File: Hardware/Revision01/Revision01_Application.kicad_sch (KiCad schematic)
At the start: 74 parts, among them J21 StrainConn, J22 StrainConn, J23 StrainConn, J24 StrainConn, J25 StrainConn, J26 StrainConn, J27 StrainConn, J28 StrainConn, J4 Conn_01x03, Q3 NMOS, Q4 PMOS, Q6 PMOS, U2 MRF89XAM9AT-I/RM, U4 ICM-45605

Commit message: random stuff added
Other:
- note added: "https://www.digikey.ca/en/products/detail/analog-devices-inc/ADA4254ARUZ-R7/11483491"
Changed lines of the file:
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@@
+		)
+	)
+	(text "https://www.digikey.ca/en/products/detail/analog-devices-inc/ADA4254ARUZ-R7/11483491\n"
+		(exclude_from_sim no)
+		(at 70.358 205.232 0)
+		(effects
+			(font
+				(size 1.4986 1.4986)
+			)
 		)
 	)

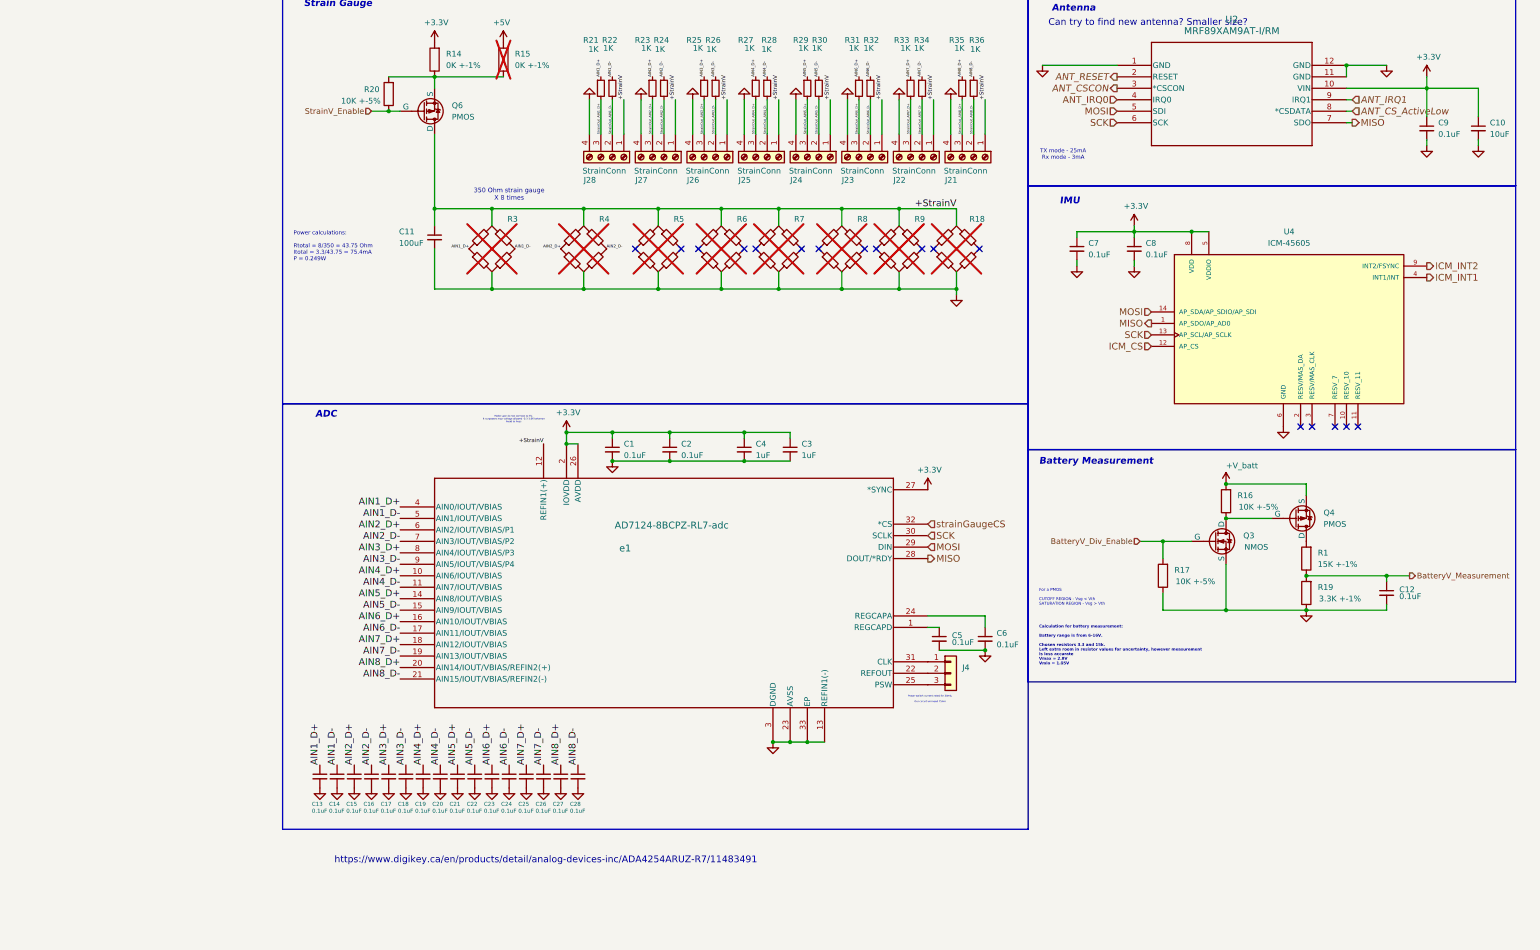
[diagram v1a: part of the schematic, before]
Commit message: some feedback implemented, MISO/MOSI SIWTCHED, GPIO_USB_5V FIXED, COMMENTS REGARDING ALTERNATIVE ADC's, and PCB CONNECTED TO EXTERNAL GND added
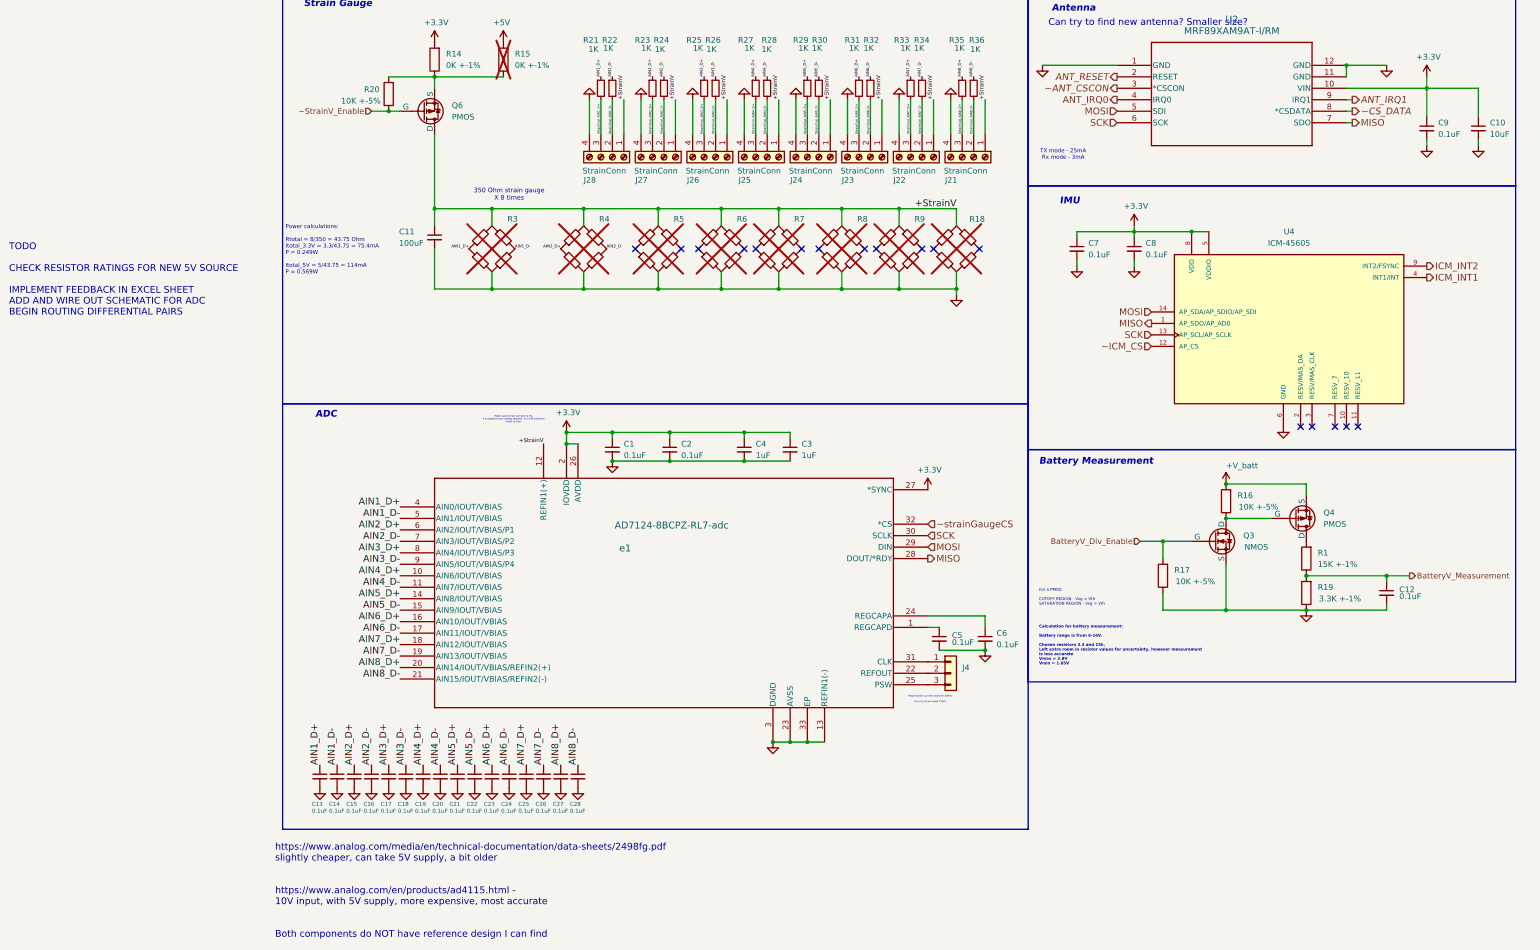
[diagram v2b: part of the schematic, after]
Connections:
- net ANT_CSCON renamed ~ANT_CSCON
- net ANT_CS_ActiveLow renamed ~CS_DATA
- net ICM_CS renamed ~ICM_CS
- net StrainV_Enable renamed ~StrainV_Enable
- net strainGaugeCS renamed ~strainGaugeCS
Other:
- note added: "Power calculations: Rtotal = 8/350 = 43.75 Ohm Itotal_3.3V = 3.3/43.75 = 75.4mA P = 0.249W Itotal_5V = 5/43.75 = 114mA P = 0.569W"
- note added: "TODO CHECK RESISTOR RATINGS FOR NEW 5V SOURCE IMPLEMENT FEEDBACK IN EXCEL SHEET ADD AND WIRE OUT SCHEMATIC FOR ADC BEGIN ROUTING DIFFERENTIAL PAIRS"
- note added: "https://www.analog.com/media/en/technical-documentation/data-sheets/2498fg.pdf slightly cheaper, can take 5V supply, a bit older https://www.analog.com/en/products/ad4115.html - 10V input, with 5V supply, more expensive, most accurate Both components do NOT have reference design I can find"
- note removed: "Power calculations: Rtotal = 8/350 = 43.75 Ohm Itotal = 3.3/43.75 = 75.4mA P = 0.249W"
- note removed: "https://www.digikey.ca/en/products/detail/analog-devices-inc/ADA4254ARUZ-R7/11483491"
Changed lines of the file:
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@@
+		)
+	)
+	(text "https://www.analog.com/media/en/technical-documentation/data-sheets/2498fg.pdf\nslightly cheaper, can take 5V supply, a bit older\n\n\nhttps://www.analog.com/en/products/ad4115.html - \n10V input, with 5V supply, more expensive, most accurate\n\n\nBoth components do NOT have reference design I can find\n"
+		(exclude_from_sim no)
+		(at 10.414 212.09 0)
+		(effects
+			(font
+				(size 1.4986 1.4986)
+			)
+			(justify left)
 		)
 	)
@@
 			(font
 				(size 1.016 1.016)
-			)
-		)
-	)
-	(text "https://www.digikey.ca/en/products/detail/analog-devices-inc/ADA4254ARUZ-R7/11483491\n"
-		(exclude_from_sim no)
-		(at 70.358 205.232 0)
-		(effects
-			(font
-				(size 1.4986 1.4986)
 			)
 		)
@@
 		)
 	)
-	(text "Power calculations:\n\nRtotal = 8/350 = 43.75 Ohm\nItotal = 3.3/43.75 = 75.4mA\nP = 0.249W"
+	(text "Power calculations:\n\nRtotal = 8/350 = 43.75 Ohm\nItotal_3.3V = 3.3/43.75 = 75.4mA\nP = 0.249W\n\nItotal_5V = 5/43.75 = 114mA\nP = 0.569W"
 		(exclude_from_sim no)
-		(at 14.478 69.342 0)
+		(at 12.7 70.104 0)
 		(effects
 			(font
@@
 				(size 1.4986 1.4986)
 			)
+		)
+	)
+	(text "TODO\n\nCHECK RESISTOR RATINGS FOR NEW 5V SOURCE\n\nIMPLEMENT FEEDBACK IN EXCEL SHEET\nADD AND WIRE OUT SCHEMATIC FOR ADC\nBEGIN ROUTING DIFFERENTIAL PAIRS"
+		(exclude_from_sim no)
+		(at -48.514 76.708 0)
+		(effects
+			(font
+				(size 1.4986 1.4986)
+			)
+			(justify left)
 		)
 	)
@@
 		)
 	)
-	(hierarchical_label "ANT_CS_ActiveLow"
-		(shape input)
+	(hierarchical_label "~CS_DATA"
+		(shape output)
 		(at 248.92 39.37 0)
 		(effects
@@
 	)
 	(hierarchical_label "ANT_IRQ1"
-		(shape input)
+		(shape output)
 		(at 248.92 36.83 0)
 		(effects
@@
 		)
 	)
-	(hierarchical_label "StrainV_Enable"
+	(hierarchical_label "~StrainV_Enable"
 		(shape input)
 		(at 31.75 39.37 180)
@@
 		)
 	)
-	(hierarchical_label "strainGaugeCS"
+	(hierarchical_label "~strainGaugeCS"
 		(shape input)
 		(at 154.94 130.81 0)
@@
 		)
 	)
-	(hierarchical_label "ICM_CS"
+	(hierarchical_label "~ICM_CS"
 		(shape input)
 		(at 204.47 91.44 180)
@@
 	)
 	(hierarchical_label "ANT_IRQ0"
-		(shape input)
+		(shape output)
 		(at 196.85 36.83 180)
 		(effects
@@
 		)
 	)
-	(hierarchical_label "ANT_CSCON"
+	(hierarchical_label "~ANT_CSCON"
 		(shape output)
 		(at 196.85 34.29 180)

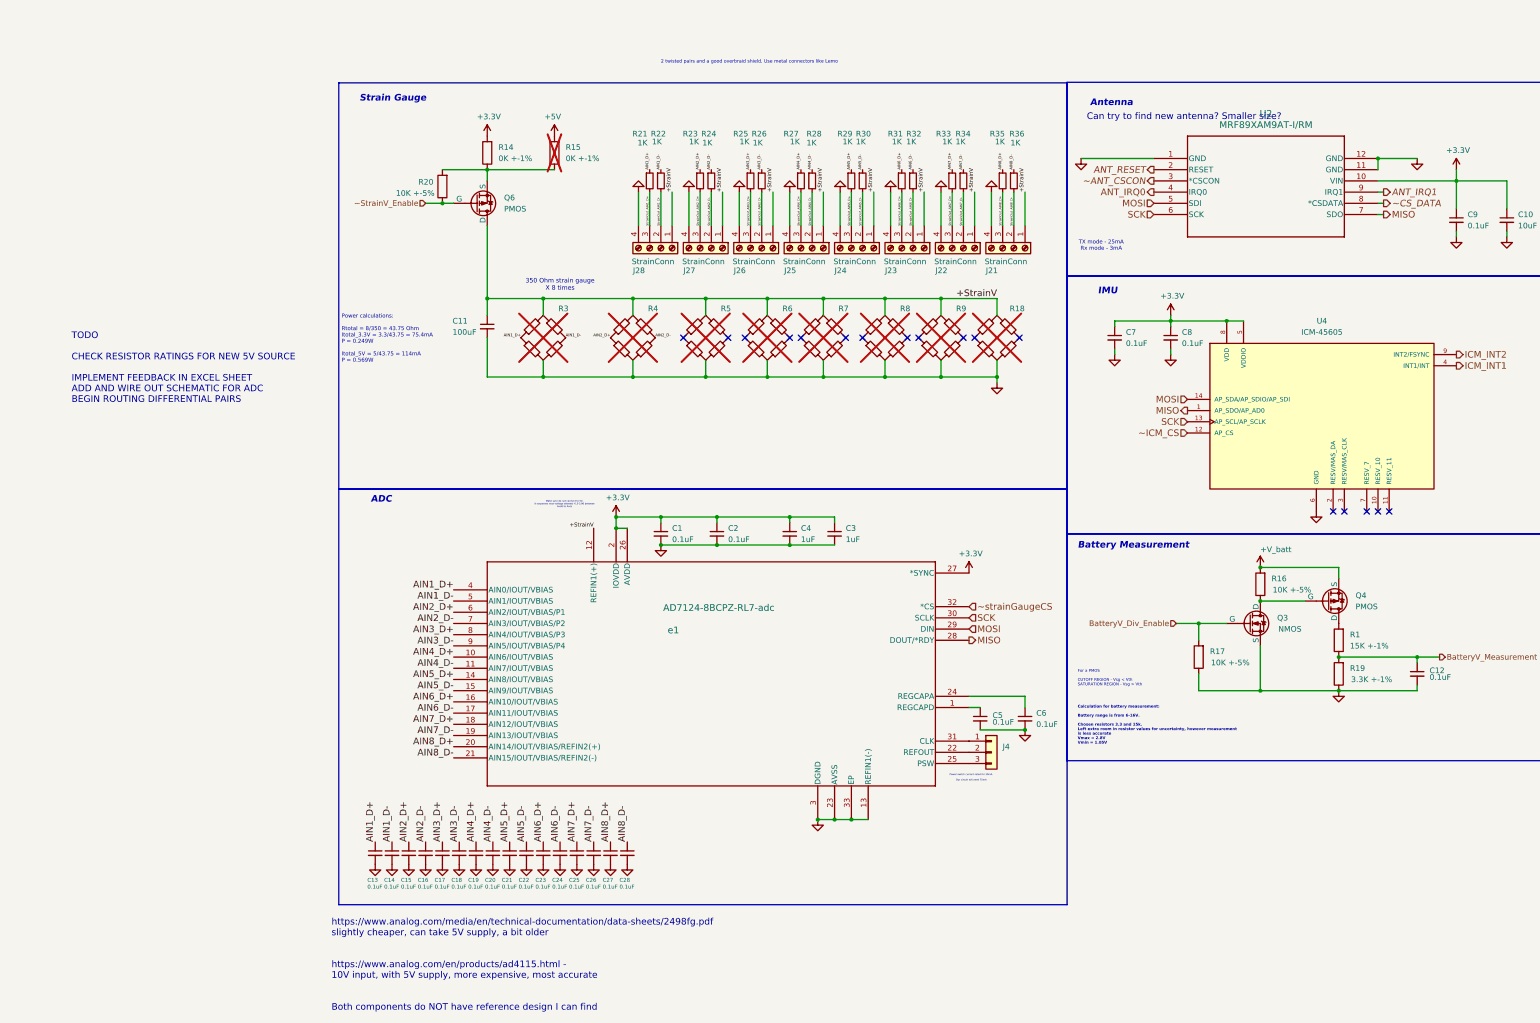
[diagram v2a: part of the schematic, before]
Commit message: Implemented new more reliable design utilizing instrumentation amplifiers
Changed RESISTORS for new Power requirements
Added prototype features of breathing cube to test out.
Removed MCU sheet, as moving pins around was getting too messy
Picked out Instrumentation OP-AMP, INA331 or INA2331
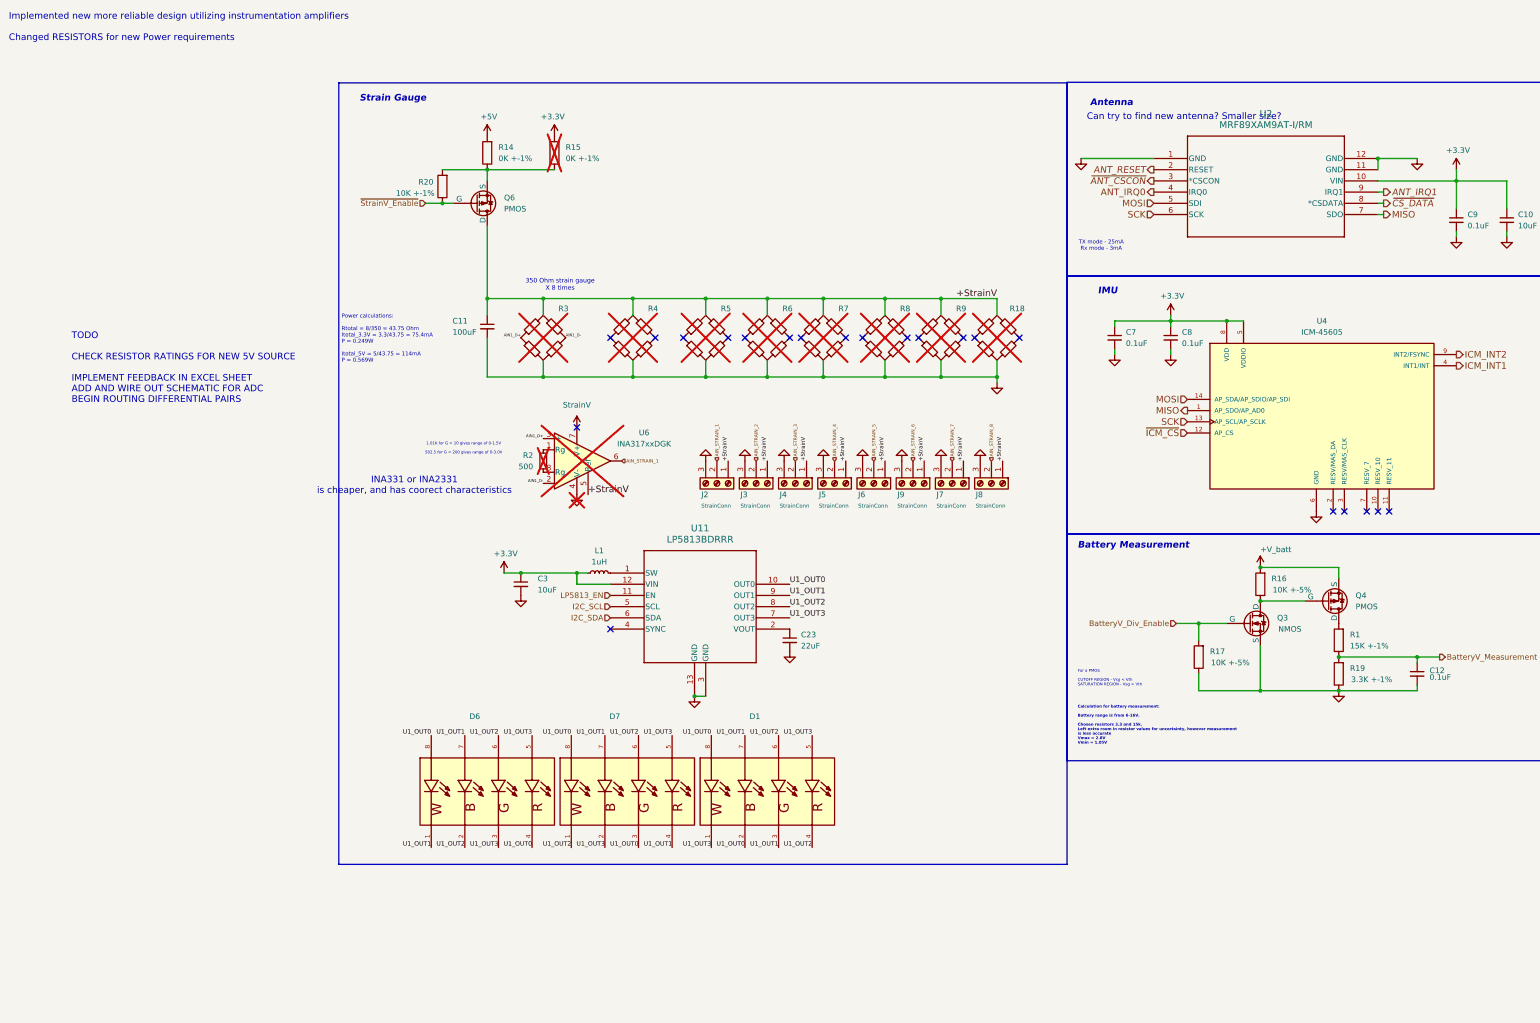
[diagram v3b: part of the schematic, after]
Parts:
- removed C1, C13, C14, C15, C16, C17, C18, C19, C2, C20, C21, C22, C24, C25, C26, C27, C28, C5, C6: 0.1uF, Capacitor_SMD:C_0402_1005Metric_Pad0.74x0.62mm_HandSolder, symbol Device:C_Small
- removed C4: 1uF, Capacitor_SMD:C_0805_2012Metric, symbol Device:C_Small
- removed J21, J22, J23, J24, J25, J26, J27, J28: StrainConn, 691137710004:691137710004, symbol Connector:Screw_Terminal_01x04
- removed J4: Conn_01x03, Connector_PinHeader_2.54mm:PinHeader_1x03_P2.54mm_Vertical, symbol Connector_Generic:Conn_01x03
- removed R21, R22, R23, R24, R25, R26, R27, R28, R29, R30, R31, R32, R33, R34, R35, R36: 1K, Resistor_SMD:R_0402_1005Metric_Pad0.72x0.64mm_HandSolder, symbol Device:R_Small
- removed e1: AD7124-8BCPZ-RL7-adc, AD7124-8BCPZ-RL7-adc:CP-32-12_ADI-L, symbol AD7124-8BCPZ-RL7-adc:AD7124-8BCPZ-RL7
- added D1, D6, D7: RGBW_LED, RGBW:SOL120P540X160-8N, symbol RGBW LED:OSFW4BS8C1A
- added J2, J3, J4, J5, J6, J7, J8, J9: StrainConn, 691137710003:691137710003, symbol Connector:Screw_Terminal_01x03
- added L1: 1uH, Inductor_SMD:L_0201_0603Metric_Pad0.64x0.40mm_HandSolder, symbol Device:L_Small
- added R2: 500, Resistor_SMD:R_0603_1608Metric_Pad0.98x0.95mm_HandSolder, symbol Device:R_Small
- added U11: LP5813BDRRR, Package_SON:WSON-12-1EP_3x3mm_P0.5mm_EP1.5x2.5mm, symbol LP5813BD:LP5813BDRRR
- added U6: INA317xxDGK, Package_SO:VSSOP-8_3x3mm_P0.65mm, symbol INA317:INA333xxDGK
- C23: value 0.1uF -> 22uF; footprint Capacitor_SMD:C_0402_1005Metric_Pad0.74x0.62mm_HandSolder -> Capacitor_SMD:C_0603_1608Metric_Pad1.08x0.95mm_HandSolder; Distributor link https://www.digikey.ca/en/products/detail/yageo/CC0805JRNPO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 -> (none); Manufacturer Samsung Electro-Mechanics -> (none); Manufacturer Part Number CL05B104KA5NNNC -> (none); Price per unit 0.12 -> (none); Quantity 23 -> (none)
- C3: value 1uF -> 10uF; footprint Capacitor_SMD:C_0805_2012Metric -> Capacitor_SMD:C_0402_1005Metric_Pad0.74x0.62mm_HandSolder; Distributor link https://www.digikey.ca/en/products/detail/vishay-sprague/TL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 -> (none); Manufacturer Part Number TL8W9105M016C -> (none); Price per unit 0.99 -> (none); Quantity 2 -> (none)
- R14, R15: footprint Capacitor_SMD:C_0805_2012Metric -> Resistor_SMD:R_1206_3216Metric_Pad1.30x1.75mm_HandSolder; Distributor link https://www.digikey.ca/en/products/detail/panasonic-electro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 -> https://www.digikey.ca/en/products/detail/vishay-dale/RCL06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; Manufacturer Part Number ERJ-6DSFR20V -> RCL06120000Z0EA
- R16, R17: footprint Resistor_SMD:R_0805_2012Metric -> Resistor_SMD:R_2512_6332Metric_Pad1.40x3.35mm_HandSolder; Manufacturer Part Number RC0805JR-0710KL -> CRGCQ2512F10K
- R20: value 10K +-5% -> 10K +-1%; footprint Resistor_SMD:R_0805_2012Metric -> Resistor_SMD:R_2512_6332Metric_Pad1.40x3.35mm_HandSolder; Distributor link https://www.digikey.ca/en/products/detail/yageo/RC0805FR-07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 -> https://www.digikey.ca/en/products/detail/te-connectivity-p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; Manufacturer Part Number RC0805JR-0710KL -> CRGCQ2512F10K
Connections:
- net +3.3V: now also R15.2, L1.1, U11.12 (VIN); no longer R14.2
- net +5V: now also R14.2; no longer R15.2
- net +StrainV: now also J2.1 (Pin_1), J3.1 (Pin_1), J4.1 (Pin_1), J5.1 (Pin_1), J6.1 (Pin_1), J7.1 (Pin_1), J8.1 (Pin_1), J9.1 (Pin_1), U6.5 (Ref)
- net AIN1_D+: now also U6.3 (+)
- net AIN1_D-: now also U6.2 (-)
- net GND: now also J2.3 (Pin_3), J3.3 (Pin_3), J4.3 (Pin_3), J5.3 (Pin_3), J6.3 (Pin_3), J7.3 (Pin_3), J8.3 (Pin_3), J9.3 (Pin_3), U11.13 (GND), U11.3 (GND), U6.4 (V-)
- net AIN2_D+: no longer names the net of R4.4
- net AIN2_D-: no longer names the net of R4.2
- net AIN6_D+: no longer names the net of C23.1
- net AIN6_D+: now also U11.2 (VOUT)
- net ~ANT_CSCON renamed ~{ANT_CSCON}
- net ~CS_DATA renamed ~{CS_DATA}
- net ~ICM_CS renamed ~{ICM_CS}
- net ~StrainV_Enable renamed ~{StrainV_Enable}
- new net: L1.2, U11.1 (SW)
- new net: R2.1, U6.1 (Rg)
- new net: R2.2, U6.8 (Rg)
- new net AIN_STRAIN_1: J2.2 (Pin_2), U6.6
- new net AIN_STRAIN_2: J3.2 (Pin_2)
- new net AIN_STRAIN_3: J4.2 (Pin_2)
- new net AIN_STRAIN_4: J5.2 (Pin_2)
- new net AIN_STRAIN_5: J6.2 (Pin_2)
- new net AIN_STRAIN_6: J9.2 (Pin_2)
- new net AIN_STRAIN_7: J7.2 (Pin_2)
- new net AIN_STRAIN_8: J8.2 (Pin_2)
- new net I2C_SCL: U11.5 (SCL)
- new net I2C_SDA: U11.6 (SDA)
- new net LP5813_EN: U11.11 (EN)
- new net U1_OUT0: D1.2, D1.8, D6.4, D6.8, D7.3, D7.8, U11.10 (OUT0)
- new net U1_OUT1: D1.3, D1.7, D6.1, D6.7, D7.4, D7.7, U11.9 (OUT1)
- new net U1_OUT2: D1.4, D1.6, D6.2, D6.6, D7.1, D7.6, U11.8 (OUT2)
- new net U1_OUT3: D1.1, D1.5, D6.3, D6.5, D7.2, D7.5, U11.7 (OUT3)
- no-connect marks 17 -> 21
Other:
- note added: "1.01K for G = 10 gives range of 0-1.5V 502.5 for G = 200 gives range of 0-3.0V"
- note added: "INA331 or INA2331 is cheaper, and has coorect characteristics"
- note added: "Implemented new more reliable design utilizing instrumentation amplifiers Changed RESISTORS for new Power requirements"
- note removed: "2 twisted pairs and a good overbraid shield. Use metal connectors like Lemo"
- note removed: "ADC"
- note removed: "Make sure do not connect to 5V, It surpasses max voltage allowed -0.3-3.96 between Avdd to Avss"
- note removed: "Power-switch current rated for 30mA. Our circuit will need 75mA"
- note removed: "https://www.analog.com/media/en/technical-documentation/data-sheets/2498fg.pdf slightly cheaper, can take 5V supply, a bit older https://www.analog.com/en/products/ad4115.html - 10V input, with 5V supply, more expensive, most accurate Both components do NOT have reference design I can find"
